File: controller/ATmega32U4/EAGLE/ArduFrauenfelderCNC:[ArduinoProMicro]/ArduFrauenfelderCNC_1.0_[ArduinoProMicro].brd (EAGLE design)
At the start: 78.7 x 73.7 mm, 10 parts, among them J1 POWER_JACKPTH_LOCK

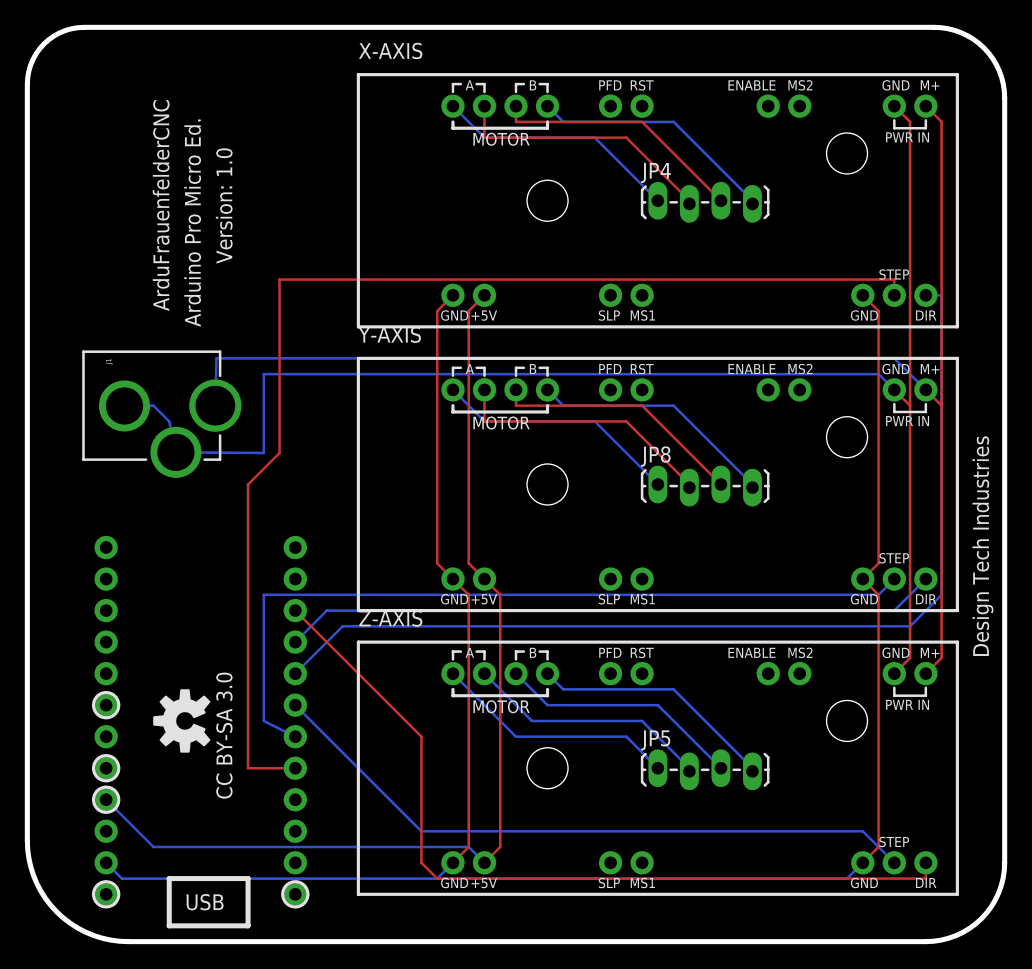
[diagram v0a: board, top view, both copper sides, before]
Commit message: Changed folder structure to be MCU specific, moving designs into 'ATmega328' and 'ATmega32U4' folders. Updated REAME.md's to reflect changes.
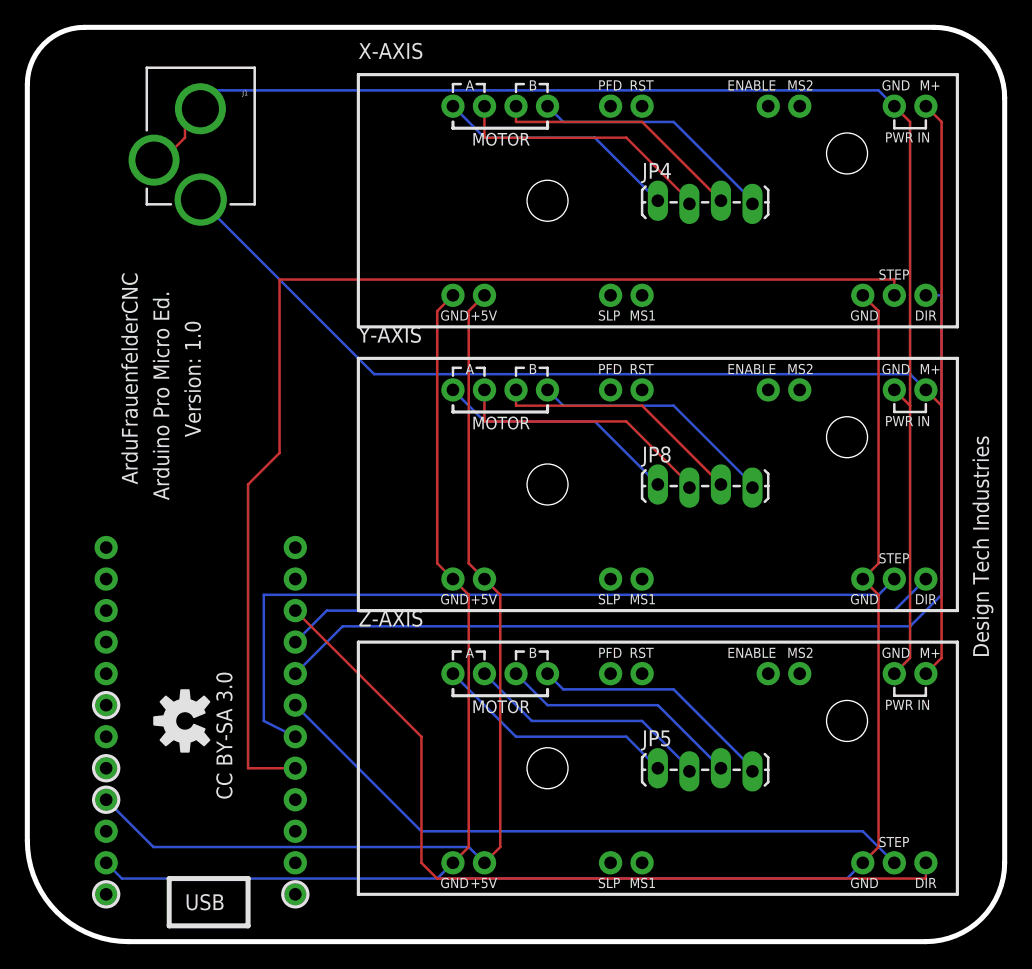
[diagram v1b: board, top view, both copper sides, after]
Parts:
- moved J1 33.0 mm to (25.4, 85.1), turned to 180 degrees
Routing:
- net N$1: track 120.0 -> 111.7 mm
- net N$4: track 110.6 -> 113.4 mm
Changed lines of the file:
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@@
 <wire x1="83.82" y1="11.43" x2="19.561965625" y2="11.43" width="0.4064" layer="20"/>
 <wire x1="19.561965625" y1="11.43" x2="11.43" y2="19.561965625" width="0.4064" layer="20" curve="-90"/>
-<text x="22.86" y="62.23" size="1.27" layer="21" rot="R90">ArduFrauenfelderCNC</text>
-<text x="25.4" y="60.96" size="1.27" layer="21" rot="R90">Arduino Pro Micro Ed.</text>
-<text x="27.94" y="66.04" size="1.27" layer="21" rot="R90">Version: 1.0</text>
+<text x="20.32" y="48.26" size="1.27" layer="21" rot="R90">ArduFrauenfelderCNC</text>
+<text x="22.86" y="46.99" size="1.27" layer="21" rot="R90">Arduino Pro Micro Ed.</text>
+<text x="25.4" y="52.07" size="1.27" layer="21" rot="R90">Version: 1.0</text>
 <text x="88.9" y="34.29" size="1.27" layer="21" rot="R90">Design Tech Industries</text>
 <text x="27.94" y="22.86" size="1.27" layer="21" rot="R90">CC BY-SA 3.0</text>
@@
 </classes>
 <designrules>
-<description language="de">&lt;b&gt;EAGLE Design Rules&lt;/b&gt;
+<description language="en">&lt;b&gt;EAGLE Design Rules&lt;/b&gt;
 &lt;p&gt;
-Die Standard-Design-Rules sind so gewählt, dass sie für
-die meisten Anwendungen passen. Sollte ihre Platine
-besondere Anforderungen haben, treffen Sie die erforderlichen
-Einstellungen hier und speichern die Design Rules unter
-einem neuen Namen ab.</description>
-<description language="en">&lt;b&gt;Laen's PCB Order Design Rules&lt;/b&gt;
-&lt;p&gt;
-Please make sure your boards conform to these design rules.</description>
+The default Design Rules have been set to cover
+a wide range of applications. Your particular design
+may have different requirements, so please make the
+necessary adjustments and save your customized
+design rules under a new name.</description>
 <param name="layerSetup" value="(1*16)"/>
-<param name="mtCopper" value="0.0356mm 0.0356mm 0.0356mm 0.0356mm 0.0356mm 0.0356mm 0.0356mm 0.0356mm 0.0356mm 0.0356mm 0.0356mm 0.0356mm 0.0356mm 0.0356mm 0.0356mm 0.0356mm"/>
-<param name="mtIsolate" value="1.5011mm 0.1499mm 0.2007mm 0.1499mm 0.2007mm 0.1499mm 0.2007mm 0.1499mm 0.2007mm 0.1499mm 0.2007mm 0.1499mm 0.2007mm 0.1499mm 0.2007mm"/>
-<param name="mdWireWire" value="6mil"/>
-<param name="mdWirePad" value="6mil"/>
-<param name="mdWireVia" value="6mil"/>
-<param name="mdPadPad" value="6mil"/>
-<param name="mdPadVia" value="6mil"/>
-<param name="mdViaVia" value="6mil"/>
-<param name="mdSmdPad" value="6mil"/>
-<param name="mdSmdVia" value="6mil"/>
-<param name="mdSmdSmd" value="6mil"/>
+<param name="mtCopper" value="0.035mm 0.035mm 0.035mm 0.035mm 0.035mm 0.035mm 0.035mm 0.035mm 0.035mm 0.035mm 0.035mm 0.035mm 0.035mm 0.035mm 0.035mm 0.035mm"/>
+<param name="mtIsolate" value="1.5mm 0.15mm 0.2mm 0.15mm 0.2mm 0.15mm 0.2mm 0.15mm 0.2mm 0.15mm 0.2mm 0.15mm 0.2mm 0.15mm 0.2mm"/>
+<param name="mdWireWire" value="8mil"/>
+<param name="mdWirePad" value="8mil"/>
+<param name="mdWireVia" value="8mil"/>
+<param name="mdPadPad" value="8mil"/>
+<param name="mdPadVia" value="8mil"/>
+<param name="mdViaVia" value="8mil"/>
+<param name="mdSmdPad" value="8mil"/>
+<param name="mdSmdVia" value="8mil"/>
+<param name="mdSmdSmd" value="8mil"/>
 <param name="mdViaViaSameLayer" value="8mil"/>
 <param name="mnLayersViaInSmd" value="2"/>
-<param name="mdCopperDimension" value="15mil"/>
-<param name="mdDrill" value="6mil"/>
+<param name="mdCopperDimension" value="10mil"/>
+<param name="mdDrill" value="8mil"/>
 <param name="mdSmdStop" value="0mil"/>
-<param name="msWidth" value="6mil"/>
-<param name="msDrill" value="13mil"/>
-<param name="msMicroVia" value="13mil"/>
+<param name="msWidth" value="8mil"/>
+<param name="msDrill" value="20mil"/>
+<param name="msMicroVia" value="9.99mm"/>
 <param name="msBlindViaRatio" value="0.5"/>
 <param name="rvPadTop" value="0.25"/>
@@
 <param name="rvMicroViaOuter" value="0.25"/>
 <param name="rvMicroViaInner" value="0.25"/>
-<param name="rlMinPadTop" value="7mil"/>
+<param name="rlMinPadTop" value="12mil"/>
 <param name="rlMaxPadTop" value="20mil"/>
-<param name="rlMinPadInner" value="7mil"/>
+<param name="rlMinPadInner" value="10mil"/>
 <param name="rlMaxPadInner" value="20mil"/>
-<param name="rlMinPadBottom" value="7mil"/>
+<param name="rlMinPadBottom" value="12mil"/>
 <param name="rlMaxPadBottom" value="20mil"/>
-<param name="rlMinViaOuter" value="7mil"/>
+<param name="rlMinViaOuter" value="10mil"/>
 <param name="rlMaxViaOuter" value="20mil"/>
-<param name="rlMinViaInner" value="7mil"/>
+<param name="rlMinViaInner" value="10mil"/>
 <param name="rlMaxViaInner" value="20mil"/>
 <param name="rlMinMicroViaOuter" value="4mil"/>
@@
 <param name="mlMinCreamFrame" value="0mil"/>
 <param name="mlMaxCreamFrame" value="0mil"/>
-<param name="mlViaStopLimit" value="0mil"/>
+<param name="mlViaStopLimit" value="25mil"/>
 <param name="srRoundness" value="0"/>
 <param name="srMinRoundness" value="0mil"/>
@@
 <element name="Y-AXIS" library="EasyDriver" package="EASYDRIVER_V44" value="EASYDRIVER_V44" x="62.23" y="48.26"/>
 <element name="Z-AXIS" library="EasyDriver" package="EASYDRIVER_V44" value="EASYDRIVER_V44" x="62.23" y="25.4"/>
-<element name="J1" library="SparkFun" package="POWER_JACK_PTH_LOCK" value="POWER_JACKPTH_LOCK" x="12.7" y="54.61" rot="R270"/>
+<element name="J1" library="SparkFun" package="POWER_JACK_PTH_LOCK" value="POWER_JACKPTH_LOCK" x="25.4" y="85.09" rot="R180"/>
 <element name="JP4" library="SparkFun" package="1X04_LOCK_LONGPADS" value="" x="62.23" y="71.12"/>
 <element name="JP5" library="SparkFun" package="1X04_LOCK_LONGPADS" value="" x="62.23" y="25.4"/>
@@
 <contactref element="J1" pad="GND"/>
 <contactref element="J1" pad="GNDBREAK"/>
-<wire x1="21.59" y1="54.61" x2="22.86" y2="53.34" width="0.2032" layer="16"/>
-<wire x1="22.86" y1="53.34" x2="23.4" y2="50.8484" width="0.2032" layer="16"/>
-<wire x1="21.59" y1="54.61" x2="19.257" y2="54.5846" width="0.2032" layer="16"/>
 <wire x1="82.55" y1="34.29" x2="81.28" y2="33.02" width="0.2032" layer="1"/>
 <wire x1="82.55" y1="54.61" x2="82.55" y2="34.29" width="0.2032" layer="1"/>
@@
 <wire x1="82.55" y1="77.47" x2="81.28" y2="78.74" width="0.2032" layer="1"/>
 <wire x1="82.55" y1="54.61" x2="82.55" y2="77.47" width="0.2032" layer="1"/>
-<wire x1="30.48" y1="57.15" x2="30.48" y2="50.8" width="0.2032" layer="16"/>
-<wire x1="80.01" y1="57.15" x2="30.48" y2="57.15" width="0.2032" layer="16"/>
-<wire x1="81.28" y1="55.88" x2="80.01" y2="57.15" width="0.2032" layer="16"/>
-<wire x1="30.48" y1="50.8" x2="23.4" y2="50.8484" width="0.2032" layer="16"/>
+<wire x1="24.13" y1="76.2" x2="22.86" y2="74.93" width="0.2032" layer="1"/>
+<wire x1="24.13" y1="77.47" x2="24.13" y2="76.2" width="0.2032" layer="1"/>
+<wire x1="22.86" y1="74.93" x2="21.6384" y2="74.39" width="0.2032" layer="1"/>
+<wire x1="24.13" y1="77.47" x2="25.3746" y2="78.533" width="0.2032" layer="1"/>
+<wire x1="26.67" y1="80.01" x2="25.4" y2="78.74" width="0.2032" layer="16"/>
+<wire x1="80.01" y1="80.01" x2="26.67" y2="80.01" width="0.2032" layer="16"/>
+<wire x1="81.28" y1="78.74" x2="80.01" y2="80.01" width="0.2032" layer="16"/>
+<wire x1="25.4" y1="78.74" x2="25.3746" y2="78.533" width="0.2032" layer="16"/>
 </signal>
 <signal name="N$4">
@@
 <wire x1="85.09" y1="77.47" x2="83.82" y2="78.74" width="0.2032" layer="1"/>
 <wire x1="85.09" y1="54.61" x2="85.09" y2="77.47" width="0.2032" layer="1"/>
-<wire x1="81.28" y1="58.42" x2="26.67" y2="58.42" width="0.2032" layer="16"/>
-<wire x1="83.82" y1="55.88" x2="81.28" y2="58.42" width="0.2032" layer="16"/>
-<wire x1="26.67" y1="58.42" x2="26.5778" y2="54.61" width="0.2032" layer="16"/>
+<wire x1="39.37" y1="57.15" x2="25.4" y2="71.12" width="0.2032" layer="16"/>
+<wire x1="82.55" y1="57.15" x2="39.37" y2="57.15" width="0.2032" layer="16"/>
+<wire x1="83.82" y1="55.88" x2="82.55" y2="57.15" width="0.2032" layer="16"/>
+<wire x1="25.4" y1="71.12" x2="25.4" y2="71.2122" width="0.2032" layer="16"/>
 </signal>
 <signal name="N$2">
